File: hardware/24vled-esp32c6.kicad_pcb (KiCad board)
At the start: 2 copper layers, 67 x 84.5 mm, 5 parts, among them J1 Conn_01x20, J2 Conn_01x20, J3 Barrel_Jack, J5 2604-1106, U1 LM2596S-5

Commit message: hardware v1
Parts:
- removed J1, J2: Conn_01x20, Connector_PinHeader_2.54mm:PinHeader_1x20_P2.54mm_Vertical
- added G***: LOGO, Library:industries_10mm, F.Cu at (152.2, 104.3)
- added Q1: AO3400A, Package_TO_SOT_SMD:SOT-23, F.Cu at (159.9, 59.2)
- added Q2: AO3400A, Package_TO_SOT_SMD:SOT-23, F.Cu at (154.9, 59.2)
- added Q3: AO3400A, Package_TO_SOT_SMD:SOT-23, F.Cu at (149.9, 59.2)
- added Q4: AO3400A, Package_TO_SOT_SMD:SOT-23, F.Cu at (144.9, 59.2)
- added Q5: AO3400A, Package_TO_SOT_SMD:SOT-23, F.Cu at (139.9, 59.2)
- added R1: 100, Resistor_SMD:R_0201_0603Metric, F.Cu at (138.7, 84.4)
- added R10: 10k, Resistor_SMD:R_0201_0603Metric, F.Cu at (141.2, 56.5)
- added R2: 10k, Resistor_SMD:R_0201_0603Metric, F.Cu at (161.2, 56.5)
- added R3: 100, Resistor_SMD:R_0201_0603Metric, F.Cu at (138.7, 86.9)
- added R4: 10k, Resistor_SMD:R_0201_0603Metric, F.Cu at (156.2, 56.5)
- added R5: 100, Resistor_SMD:R_0201_0603Metric, F.Cu at (138.7, 91.9)
- added R6: 10k, Resistor_SMD:R_0201_0603Metric, F.Cu at (151.2, 56.5)
- added R7: 100, Resistor_SMD:R_0201_0603Metric, F.Cu at (138.7, 96.9)
- added R8: 10k, Resistor_SMD:R_0201_0603Metric, F.Cu at (146.2, 56.5)
- added R9: 100, Resistor_SMD:R_0201_0603Metric, F.Cu at (138.7, 99.4)
- added U2: ~, Library:Waveshare ESP32c6, F.Cu at (152.4, 88.8)
- U1: value LM2596S-5 -> R-78E5.0-1.0; footprint Package_TO_SOT_SMD:TO-263-5_TabPin3 -> Converter_DCDC:Converter_DCDC_RECOM_R-78E-0.5_THT
- moved J3 60.6 mm to (154.0, 119.0), turned to 90 degrees
- moved U1 41.3 mm to (148.5, 116.0), turned to 180 degrees
- moved J5 32.8 mm to (164.0, 53.2), turned to 180 degrees
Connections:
- J3 pad 1: Net-(U1-VIN) -> +24V
- J3 pad 2: Net-(U1-GND) -> GND
- J5 pad 1: unconnected-(J5-1_1-Pad1) -> +24V
- J5 pad 11: unconnected-(J5-6_1-Pad11) -> WW24
- J5 pad 3: unconnected-(J5-2_1-Pad3) -> R24
- J5 pad 5: unconnected-(J5-3_1-Pad5) -> G24
- J5 pad 7: unconnected-(J5-4_1-Pad7) -> B24
- J5 pad 9: unconnected-(J5-5_1-Pad9) -> CW24
- U1 pad 1: Net-(U1-VIN) -> +24V
- U1 pad 2: +5V -> GND
- U1 pad 3: Net-(U1-GND) -> +5V
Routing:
- net Net-(Q1-G): track 0.00 -> 61.6 mm, vias 0 -> 2
- net Net-(Q4-G): track 0.00 -> 60.1 mm, vias 0 -> 2
- net Net-(Q3-G): track 0.00 -> 59.6 mm, vias 0 -> 2
- net Net-(Q2-G): track 0.00 -> 59.4 mm, vias 0 -> 2
- net Net-(Q5-G): track 0.00 -> 58.8 mm, vias 0 -> 2
- net (no net): track 32.5 -> 0.00 mm
- net Net-(U1-VIN): track 19.1 -> 0.00 mm, vias 1 -> 0
- net +5V: track 32.6 -> 15.7 mm
- net Net-(U1-GND): track 16.5 -> 0.00 mm
- net WW24: track 0.00 -> 5.05 mm
- net R24: track 0.00 -> 5.05 mm
- net G24: track 0.00 -> 5.05 mm
- net CW24: track 0.00 -> 5.05 mm
- net B24: track 0.00 -> 5.05 mm
- net R3.3: track 0.00 -> 2.72 mm
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- added copper zone on B.Cu, net +24V
- added copper zone on F.Cu, net GND
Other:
- board size 67 x 84.5 mm -> 31.4 x 85.7 mm

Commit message: hardware v2
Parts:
- removed J5: 2604-1106, Wago:CONN6_2604-1106_WAG
- added J1: 2601-1106, External:26011106, F.Cu at (159.2, 50.5)
- moved J3 51.3 mm to (151.0, 67.8)
- moved U1 51.3 mm to (141.3, 65.2), turned to -90 degrees
- moved R1 27.9 mm to (141.8, 112.2)
- moved R3 22.9 mm to (141.8, 109.6)
- moved R5 13.1 mm to (141.8, 104.7)
- moved U2 12.9 mm to (150.9, 101.6)
- moved G*** 8.30 mm to (151.1, 112.5)
- moved R7 4.05 mm to (141.8, 99.6)
- moved R9 3.80 mm to (141.8, 97.2)
- moved Q1 0.57 mm to (160.5, 59.2)
- moved Q2 0.57 mm to (155.5, 59.2)
- moved Q3 0.57 mm to (150.5, 59.2)
- moved Q4 0.57 mm to (145.5, 59.2)
- moved Q5 0.57 mm to (140.5, 59.2)
- moved R10 0.57 mm to (141.8, 56.5)
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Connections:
- U2 pad 12: CW3.3 -> G3.3
- U2 pad 13: WW3.3 -> R3.3
- U2 pad 7: R3.3 -> WW3.3
- U2 pad 8: G3.3 -> CW3.3
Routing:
- net GND: track 0.00 -> 45.3 mm
- net Net-(Q1-G): track 61.6 -> 94.7 mm
- net +5V: track 15.7 -> 48.5 mm
- net Net-(Q2-G): track 59.4 -> 86.7 mm
- net Net-(Q3-G): track 59.6 -> 79.4 mm
- net Net-(Q4-G): track 60.1 -> 69.5 mm
- net R24: track 5.05 -> 9.36 mm
- net Net-(Q5-G): track 58.8 -> 62.8 mm
- net G24: track 5.05 -> 8.96 mm
- net WW24: track 5.05 -> 8.83 mm
- net B24: track 5.05 -> 8.12 mm
- net CW24: track 5.05 -> 8.06 mm
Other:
- board size 31.4 x 85.7 mm -> 25.6 x 90.3 mm

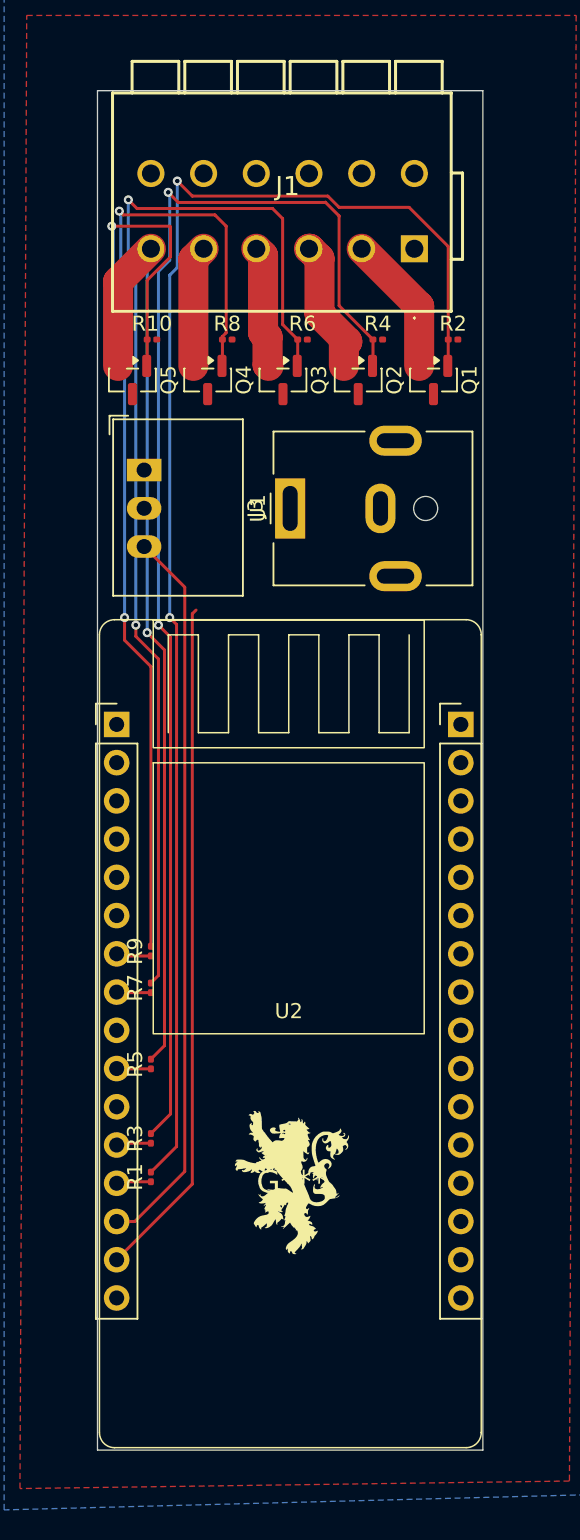
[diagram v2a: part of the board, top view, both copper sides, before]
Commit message: fix all pcb warnings and use larger resistors
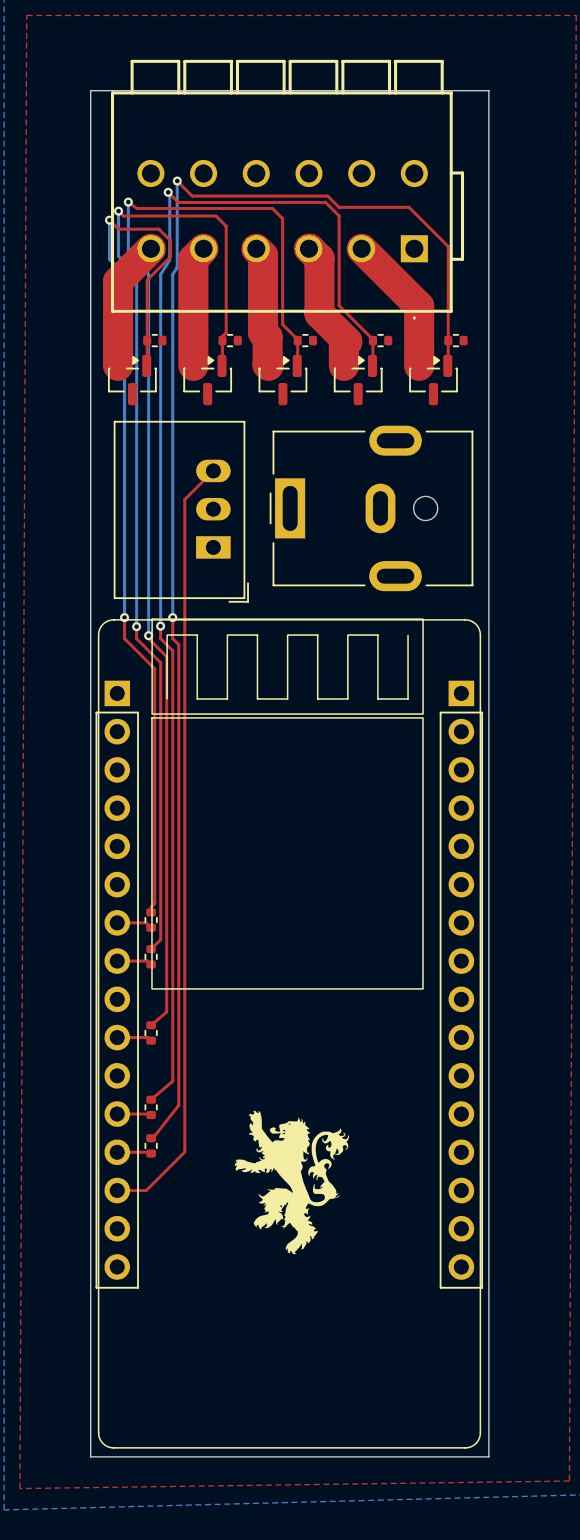
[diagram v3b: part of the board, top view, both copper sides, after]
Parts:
- R1, R10, R2, R3, R4, R5, R6, R7, R8, R9: footprint Resistor_SMD:R_0201_0603Metric -> Resistor_SMD:R_0402_1005Metric
- U2: footprint Library:Waveshare ESP32c6 -> Internal:Waveshare ESP32c6
- moved U1 6.90 mm to (145.9, 70.3), turned to 90 degrees
- moved R1 2.06 mm to (141.8, 110.1)
- moved R3 2.06 mm to (141.8, 107.5)
- moved R5 2.06 mm to (141.8, 102.6)
- moved R7 2.06 mm to (141.8, 97.5)
- moved R9 2.06 mm to (141.8, 95.1)
- moved U2 2.06 mm to (150.9, 99.6)
- moved R10 0.20 mm to (142.0, 56.6)
- moved R2 0.20 mm to (162.0, 56.6)
- moved R4 0.20 mm to (157.0, 56.6)
- moved R6 0.20 mm to (152.0, 56.6)
- moved R8 0.20 mm to (147.0, 56.6)
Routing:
- net GND: track 45.3 -> 0.00 mm
- net +5V: track 48.5 -> 51.7 mm
- net Net-(Q1-G): track 94.7 -> 92.3 mm
- net Net-(Q3-G): track 79.4 -> 77.1 mm
- net Net-(Q2-G): track 86.7 -> 84.4 mm
- net Net-(Q4-G): track 69.5 -> 67.4 mm
- net Net-(Q5-G): track 62.8 -> 61.0 mm
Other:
- board size 25.6 x 90.3 mm -> 26.4 x 90.8 mm

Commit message: update pages
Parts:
- G***: footprint Library:industries_10mm -> Internal:industries_10mm
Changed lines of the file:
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@@
 		)
 	)
-	(footprint "Library:industries_10mm"
+	(footprint "Internal:industries_10mm"
 		(layer "F.Cu")
 		(at 151.1 112.5)
@@
 			(at 0 0 0)
 			(layer "F.SilkS")
-			(hide yes)
 			(effects
 				(font

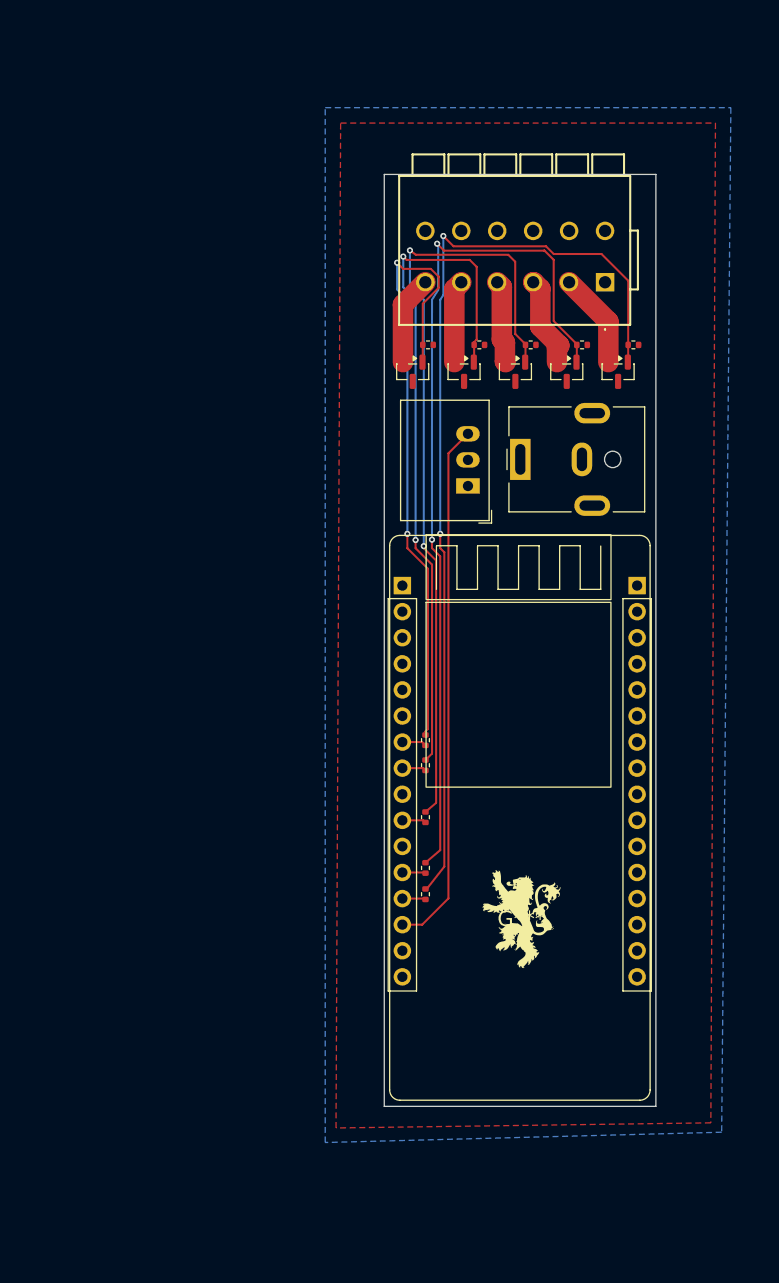
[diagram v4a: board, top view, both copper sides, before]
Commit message: add the large cap and remove the flyback diodes
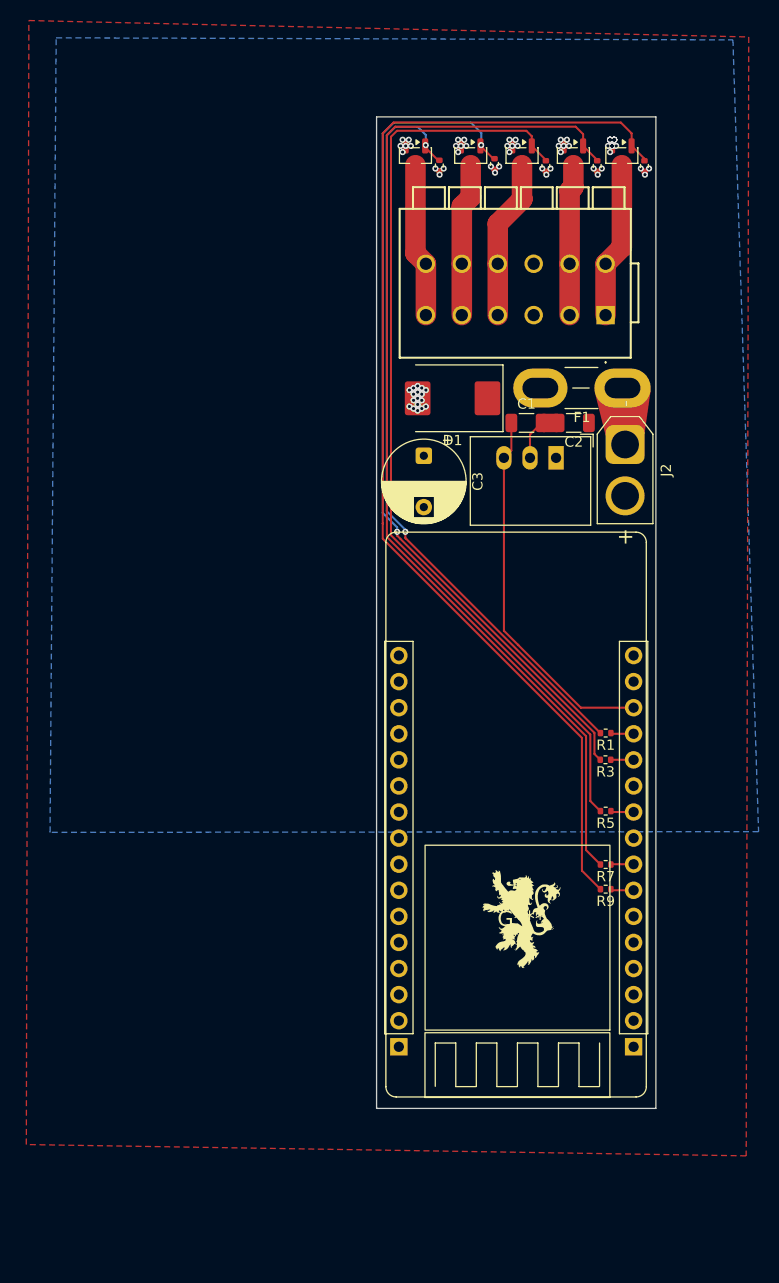
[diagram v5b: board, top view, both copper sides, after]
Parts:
- removed J3: Barrel_Jack, Connector_BarrelJack:BarrelJack_CUI_PJ-063AH_Horizontal
- added C1: C, Capacitor_SMD:C_1206_3216Metric, F.Cu at (151.6, 64.2)
- added C2: C, Capacitor_SMD:C_1206_3216Metric, F.Cu at (156.2, 64.2)
- added C3: CP, Capacitor_THT:CP_Radial_D8.0mm_P5.00mm, F.Cu at (141.6, 67.4)
- added D1: SMC, Diode_SMD:D_SMC, F.Cu at (144.4, 61.8)
- added F1: 10A, Fuse:Fuse_Blade_Mini_directSolder, F.Cu at (160.9, 60.8)
- added J2: Conn_01x02_Pin, Connector_AMASS:AMASS_XT30U-M_1x02_P5.0mm_Vertical, F.Cu at (161.2, 66.3)
- moved Q5 29.3 mm to (160.9, 38.2)
- moved Q1 28.9 mm to (140.8, 38.2)
- moved R10 27.3 mm to (163.1, 39.2), turned to 90 degrees
- moved R2 25.7 mm to (143.1, 39.1), turned to 90 degrees
- moved Q4 23.6 mm to (156.2, 38.2)
- moved R1 23.5 mm to (159.3, 94.4), turned to 180 degrees
- moved Q2 23.0 mm to (146.2, 38.2)
- moved R9 22.8 mm to (159.3, 109.6), turned to 180 degrees
- moved Q3 21.1 mm to (151.2, 38.2)
- moved R8 20.9 mm to (158.5, 39.2), turned to 90 degrees
- moved R3 20.4 mm to (159.3, 97.0), turned to 180 degrees
- moved R7 20.0 mm to (159.3, 107.2), turned to 180 degrees
- moved R4 19.6 mm to (148.5, 39.0), turned to 90 degrees
- moved R5 17.6 mm to (159.3, 102.0), turned to 180 degrees
- moved R6 17.5 mm to (153.5, 39.2), turned to 90 degrees
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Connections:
- J1 pad 1: +24V -> R24
- J1 pad 10: unconnected-(J1-5.2-Pad10) -> CW24
- J1 pad 12: unconnected-(J1-6.2-Pad12) -> WW24
- J1 pad 2: unconnected-(J1-1.2-Pad2) -> R24
- J1 pad 3: R24 -> G24
- J1 pad 4: unconnected-(J1-2.2-Pad4) -> G24
- J1 pad 5: G24 -> +24V
- J1 pad 6: unconnected-(J1-3.2-Pad6) -> +24V
- J1 pad 8: unconnected-(J1-4.2-Pad8) -> B24
- Q1 pad 2: R24 -> GND
- Q1 pad 3: GND -> WW24
- Q2 pad 2: G24 -> GND
- Q2 pad 3: GND -> CW24
- Q3 pad 2: B24 -> GND
- Q3 pad 3: GND -> B24
- Q4 pad 2: CW24 -> GND
- Q4 pad 3: GND -> G24
- Q5 pad 2: WW24 -> GND
- Q5 pad 3: GND -> R24
- R1 pad 1: R3.3 -> WW3.3
- R10 pad 1: Net-(Q5-G) -> GND
- R10 pad 2: GND -> Net-(Q5-G)
- R2 pad 1: Net-(Q1-G) -> GND
- R2 pad 2: GND -> Net-(Q1-G)
- R3 pad 1: G3.3 -> CW3.3
- R4 pad 1: Net-(Q2-G) -> GND
- R4 pad 2: GND -> Net-(Q2-G)
- R6 pad 1: Net-(Q3-G) -> GND
- R6 pad 2: GND -> Net-(Q3-G)
- R7 pad 1: CW3.3 -> G3.3
- R8 pad 1: Net-(Q4-G) -> GND
- R8 pad 2: GND -> Net-(Q4-G)
- R9 pad 1: WW3.3 -> R3.3
- U2 pad 12: G3.3 -> CW3.3
- U2 pad 13: R3.3 -> WW3.3
- U2 pad 7: WW3.3 -> R3.3
- U2 pad 8: CW3.3 -> G3.3
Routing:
- net Net-(Q5-G): track 61.0 -> 110.7 mm, vias 2 -> 0
- net Net-(Q4-G): track 67.4 -> 102.6 mm, vias 2 -> 0
- net Net-(Q1-G): track 92.3 -> 74.2 mm
- net +5V: track 51.7 -> 36.3 mm
- net Net-(Q3-G): track 77.1 -> 91.2 mm, vias 2 -> 0
- net B24: track 8.12 -> 15.6 mm
- net CW24: track 8.06 -> 15.0 mm
- net WW24: track 8.83 -> 15.0 mm
- net R24: track 9.36 -> 15.3 mm
- net G24: track 8.96 -> 14.8 mm
- net GND: track 0.00 -> 4.92 mm, vias 0 -> 70
- net Net-(Q2-G): track 84.4 -> 83.3 mm
- added copper zone on F.Cu, net +24V
- added copper zone on B.Cu, net GND
- removed copper zone on B.Cu, net +24V
- removed copper zone on F.Cu, net GND
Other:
- board size 26.4 x 90.8 mm -> 27.2 x 96.5 mm

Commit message: final version!
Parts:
- moved D1 20.7 mm to (156.2, 78.8), turned to 0 degrees
- moved C3 20.3 mm to (161.8, 69.8), turned to 180 degrees
- moved J2 15.1 mm to (146.7, 62.0), turned to 180 degrees
- moved U1 12.9 mm to (142.4, 72.0), turned to 0 degrees
- moved F1 7.99 mm to (153.1, 62.0), turned to 0 degrees
- moved C1 7.92 mm to (152.2, 72.1), turned to 90 degrees
- moved C2 5.19 mm to (152.2, 67.5), turned to -90 degrees
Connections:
- J1 pad 1: R24 -> +24V
- J1 pad 2: R24 -> +24V
- J1 pad 3: G24 -> R24
- J1 pad 4: G24 -> R24
- J1 pad 5: +24V -> G24
- J1 pad 6: +24V -> G24
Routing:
- net /V_IN: track 0.00 -> 6.35 mm
- net GND: track 4.92 -> 1.05 mm, vias 70 -> 77
- net +5V: track 36.3 -> 34.4 mm
- net G24: track 14.8 -> 16.2 mm
- net R24: track 15.3 -> 16.7 mm

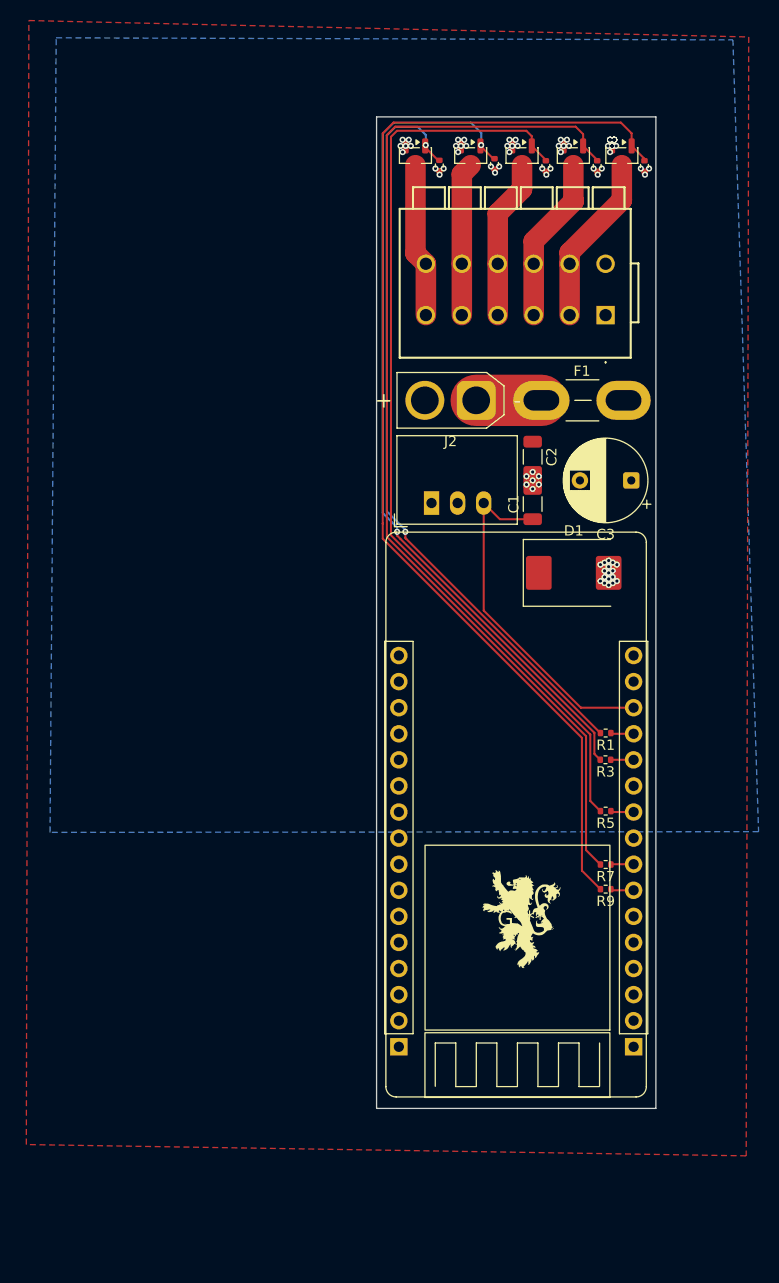
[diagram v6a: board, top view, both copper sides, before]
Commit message: fix warnings and add part numbers
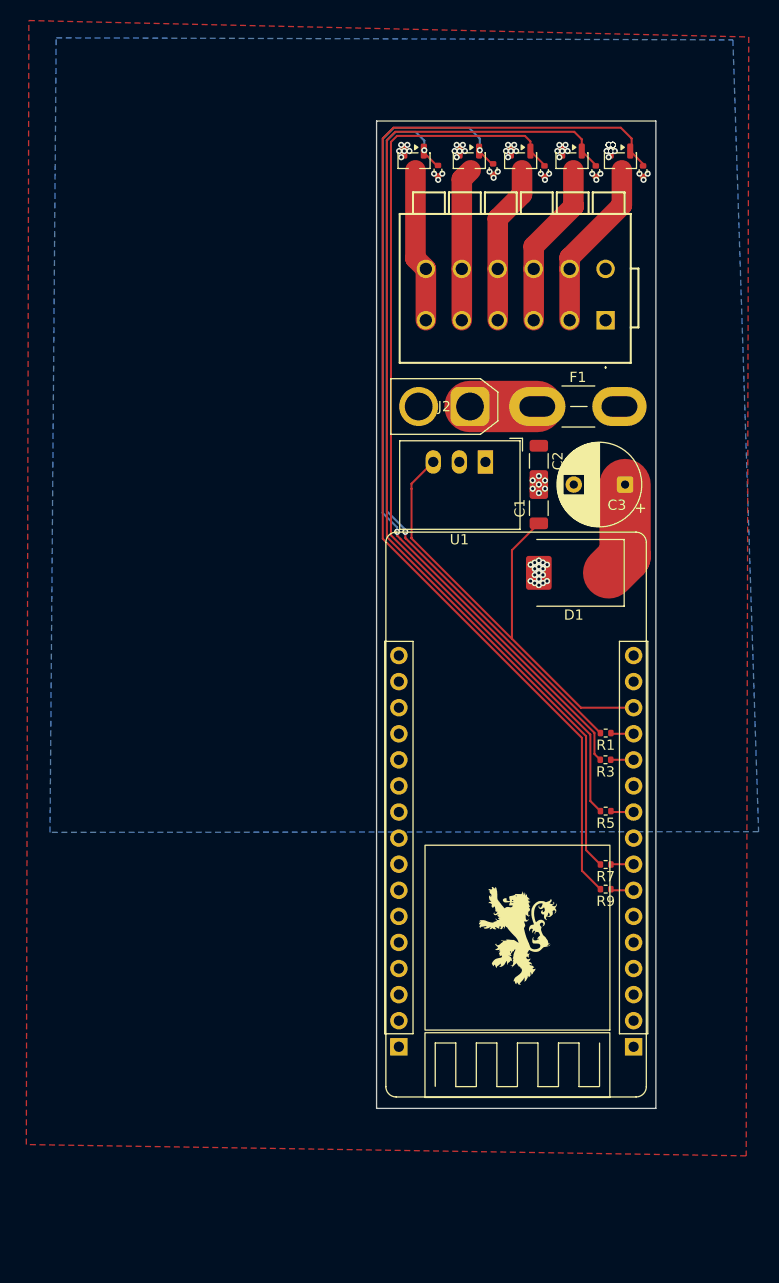
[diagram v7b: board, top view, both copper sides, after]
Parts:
- moved U1 6.60 mm to (147.6, 68.0), turned to 180 degrees
- moved G*** 1.65 mm to (150.7, 114.1)
- moved J2 0.85 mm to (146.1, 62.6)
- moved C1 0.72 mm to (152.8, 72.5)
- moved C2 0.72 mm to (152.8, 67.9)
- moved F1 0.72 mm to (152.7, 62.6)
- moved C3 0.72 mm to (161.2, 70.2)
- moved R10 0.52 mm to (162.9, 39.7)
- moved R2 0.52 mm to (143.0, 39.6)
- moved R4 0.52 mm to (148.3, 39.5)
- moved R6 0.52 mm to (153.3, 39.7)
- moved R8 0.52 mm to (158.3, 39.7)
- moved Q1 0.52 mm to (140.7, 38.7)
- moved Q2 0.52 mm to (146.0, 38.7)
- moved Q3 0.52 mm to (151.0, 38.7)
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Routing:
- net +5V: track 34.4 -> 49.1 mm
- net +24V: track 0.00 -> 9.26 mm
- net Net-(Q2-G): track 83.3 -> 82.6 mm
- net Net-(Q1-G): track 74.2 -> 73.5 mm
- net Net-(Q3-G): track 91.2 -> 90.6 mm
- net Net-(Q4-G): track 102.6 -> 101.9 mm
- net Net-(Q5-G): track 110.7 -> 110.2 mm
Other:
- board size 27.2 x 96.5 mm -> 27.2 x 96.1 mm
